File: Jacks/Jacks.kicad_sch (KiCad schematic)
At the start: 19 parts, among them J101 Barrel_Jack_Switch, J102 AudioJack2_Ground, J103 AudioJack2_Ground, J104 Conn_02x05_Odd_Even, Q101 DMC3071LVT, Q102 BC846

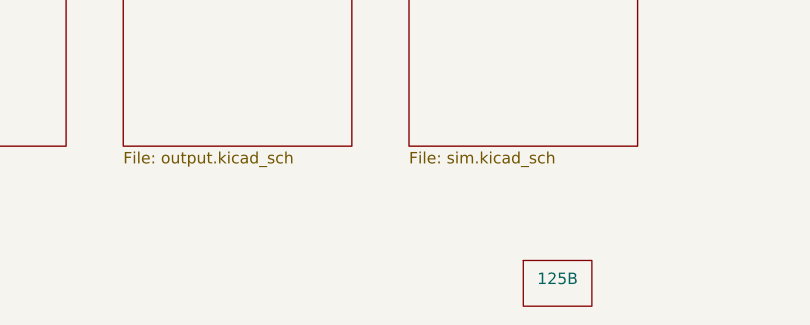
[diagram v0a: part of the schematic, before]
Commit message: Connect up the jack board with the new 1590B model
Note that I picked the Z offset as just a random number that looks
roughly right for the jack board, but with the different boards at
different offsets, I don't know that you can ever get it right.

But it's all a pretty visualization of how the board doesn't quite fit
in a 1590B.

Signed-off-by: Linus Torvalds <torvalds@linux-foundation.org>
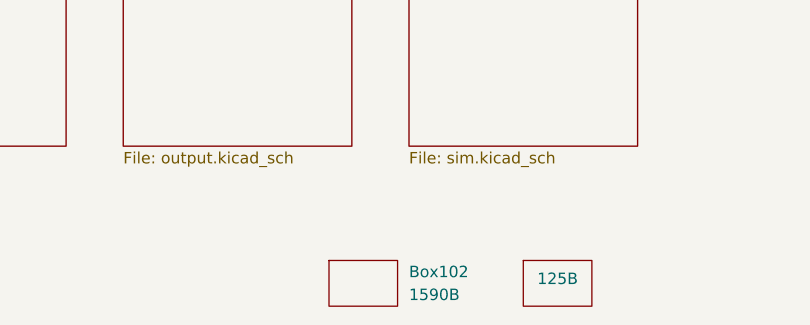
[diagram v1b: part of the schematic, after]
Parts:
- added Box102: 1590B, Mylib:1590B, symbol Mylib:Enclosure_1590B
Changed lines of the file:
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@@
+	)
+	(symbol
+		(lib_id "Mylib:Enclosure_1590B")
+		(at 248.92 172.72 0)
+		(unit 1)
+		(exclude_from_sim yes)
+		(in_bom yes)
+		(on_board yes)
+		(dnp no)
+		(fields_autoplaced yes)
+		(property "Reference" "Box102"
+			(at 254 172.7199 0)
+			(effects
+				(font
+					(size 1.27 1.27)
+				)
+				(justify left)
+			)
+		)
+		(property "Value" "1590B"
+			(at 254 175.2599 0)
+			(effects
+				(font
+					(size 1.27 1.27)
+				)
+				(justify left)
+			)
+		)
+		(property "Footprint" "Mylib:1590B"
+			(at 248.92 170.18 0)
+			(effects
+				(font
+					(size 1.27 1.27)
+				)
+				(hide yes)
+			)
+		)
+		(property "Datasheet" "https://www.hammfg.com/pdf/1590B.pdf"
+			(at 248.92 180.34 0)
+			(effects
+				(font
+					(size 1.27 1.27)
+				)
+				(hide yes)
+			)
+		)
+		(property "Description" "Guitar pedal enclosure"
+			(at 248.92 177.8 0)
+			(effects
+				(font
+					(size 1.27 1.27)
+				)
+				(hide yes)
+			)
+		)
+		(instances
+			(project ""
+				(path "/9e337e0b-885b-4d2b-99a2-62cdd082c615"
+					(reference "Box102")
+					(unit 1)
+				)
+			)
+		)
 	)
 	(symbol

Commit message: Add ugly 3d model to DC barrel jack
Based on the Würth datasheet:

   https://www.we-online.com/components/products/datasheet/694106301002.pdf

and my stumbling attempts at generating a STEP file with openscad and
freecad.

This time I couldn't get rid of the "hole turns into a plug" problem
with the freecad STEP file exprt, so once again the model looks fine in
both openscad and in freecad, but the STEP export just looks wrong with
no hole for the power plug.

There's some subtle order of operations bug thing going on.  But I'll
use it as a way to distract from the ugliness of the model: everybody
will just look at the lack of hole for the plug, and overlook the harsh
edges.

Also: dazzle them with colors.  That's the trick.  Nobody will question
my mad design skillz when it's colorized and there are obvious freecad
export issues.

Signed-off-by: Linus Torvalds <torvalds@linux-foundation.org>
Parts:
- J101: footprint Connector_BarrelJack:BarrelJack_Wuerth_6941xx301002 -> Mylib:Wurth WR-DC 2.1mm Power Jack
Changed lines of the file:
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@@
 			)
 		)
-		(property "Footprint" "Connector_BarrelJack:BarrelJack_Wuerth_6941xx301002"
+		(property "Footprint" "Mylib:Wurth WR-DC 2.1mm Power Jack"
 			(at 33.02 50.546 0)
 			(effects

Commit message: Another try at cleaning up project path handling
The removed TOPLEVEL hackery also tried to deal with the problem of
finding the spice models for simulation, which had the same confusion
with project-specific files and no sane kicad model that I could find
for it.

This attempts to deal with it by just making a 'spice' symlink from the
"kicad project" directory to the "real project" directory, and dealing
with the spice model paths that way.

Signed-off-by: Linus Torvalds <torvalds@linux-foundation.org>
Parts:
- Q102: symbol Transistor_BJT:BC846 -> Mylib:BC846
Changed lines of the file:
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@@
 			)
 		)
-		(property "Sim.Library" "${KIPRJMOD}/../symbols/DMC3071LVT.lib"
+		(property "Sim.Library" "spice/DMC3071LVT.lib"
 			(at 49.53 105.41 0)
 			(effects
@@
 			)
 		)
-		(property "Sim.Library" "${KIPRJMOD}/../symbols/DMC3071LVT.lib"
+		(property "Sim.Library" "spice/DMC3071LVT.lib"
 			(at 49.53 129.54 0)
 			(effects
@@
 	)
 	(symbol
-		(lib_id "Transistor_BJT:BC846")
+		(lib_id "Mylib:BC846")
 		(at 229.87 74.93 0)
 		(unit 1)
@@
 		)
 		(property "Footprint" "Package_TO_SOT_SMD:SOT-23"
-			(at 234.95 76.835 0)
-			(effects
-				(font
-					(size 1.27 1.27)
-					(italic yes)
-				)
-				(justify left)
-				(hide yes)
-			)
-		)
-		(property "Datasheet" "https://assets.nexperia.com/documents/data-sheet/BC846_SER.pdf"
-			(at 229.87 74.93 0)
-			(effects
-				(font
-					(size 1.27 1.27)
-				)
-				(justify left)
-				(hide yes)
-			)
-		)
-		(property "Description" "0.1A Ic, 65V Vce, NPN Transistor, SOT-23"
-			(at 229.87 74.93 0)
-			(effects
-				(font
-					(size 1.27 1.27)
-				)
-				(hide yes)
-			)
-		)
-		(property "Sim.Library" "/home/torvalds/KiCad/sim/BC846.txt"
-			(at 229.87 74.93 0)
-			(effects
-				(font
-					(size 1.27 1.27)
-				)
-				(hide yes)
-			)
-		)
-		(property "Sim.Name" "BC846"
-			(at 229.87 74.93 0)
-			(effects
-				(font
-					(size 1.27 1.27)
-				)
+			(at 229.87 62.23 0)
+			(effects
+				(font
+					(size 1.27 1.27)
+				)
+				(hide yes)
+			)
+		)
+		(property "Datasheet" "https://assets.nexperia.com/documents/data-sheet/BC846X-Q_SER.pdf"
+			(at 229.87 87.63 0)
+			(effects
+				(font
+					(size 1.27 1.27)
+				)
+				(hide yes)
+			)
+		)
+		(property "Description" "NPN transistor, base/emitter/collector"
+			(at 229.87 59.69 0)
+			(effects
+				(font
+					(size 1.27 1.27)
+				)
+				(hide yes)
+			)
+		)
+		(property "Sim.Library" "spice/BC846A.lib"
+			(at 229.87 95.25 0)
+			(effects
+				(font
+					(size 1.27 1.27)
+				)
+				(hide yes)
+			)
+		)
+		(property "Sim.Name" "BC846A"
+			(at 231.14 90.17 0)
+			(effects
+				(font
+					(size 1.27 1.27)
+				)
+				(justify left)
 				(hide yes)
 			)
 		)
 		(property "Sim.Device" "SUBCKT"
-			(at 229.87 74.93 0)
-			(effects
-				(font
-					(size 1.27 1.27)
-				)
-				(hide yes)
-			)
-		)
-		(property "Sim.Pins" "1=2 2=3 3=1"
-			(at 229.87 74.93 0)
-			(effects
-				(font
+			(at 228.6 90.17 0)
+			(effects
+				(font
+					(size 1.27 1.27)
+				)
+				(justify right)
+				(hide yes)
+			)
+		)
+		(property "Sim.Pins" "1=B 2=E 3=C"
+			(at 229.87 92.71 0)
+			(effects
+				(font
